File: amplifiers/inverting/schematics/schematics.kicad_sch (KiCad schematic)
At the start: 5 parts, among them J1 15V, U1 LM741

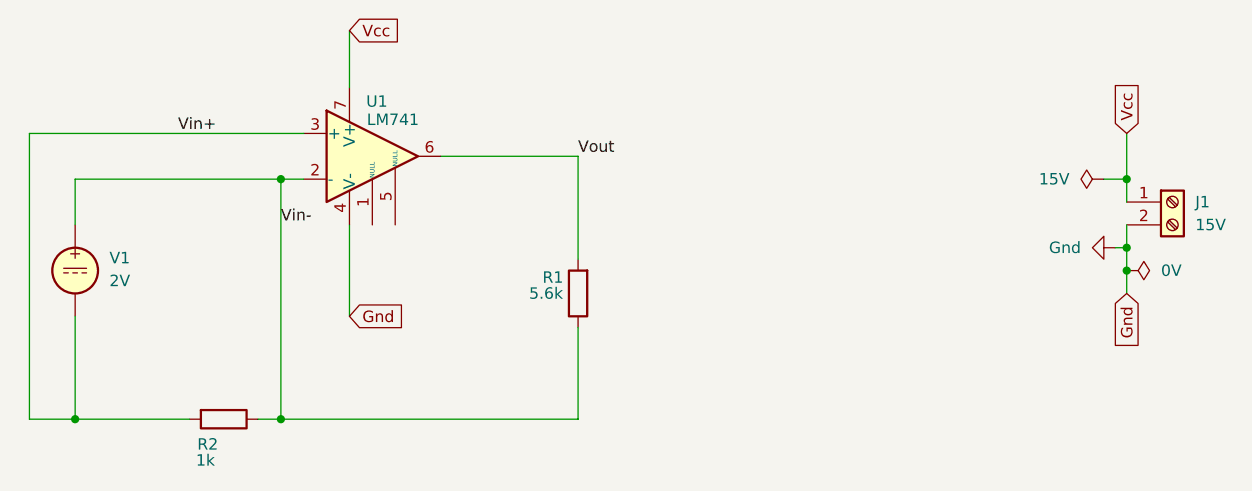
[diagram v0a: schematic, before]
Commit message: docs: add inverting amplifier practical measurements and schematics
Adds practical measurement data and schematics for the inverting
amplifier project. Includes oscilloscope screenshots and measurement
spreadsheet to enhance documentation and provide reference for future
work. Updates GitHub Pages to reflect these additions.

Breaking changes: None

Resolves: None
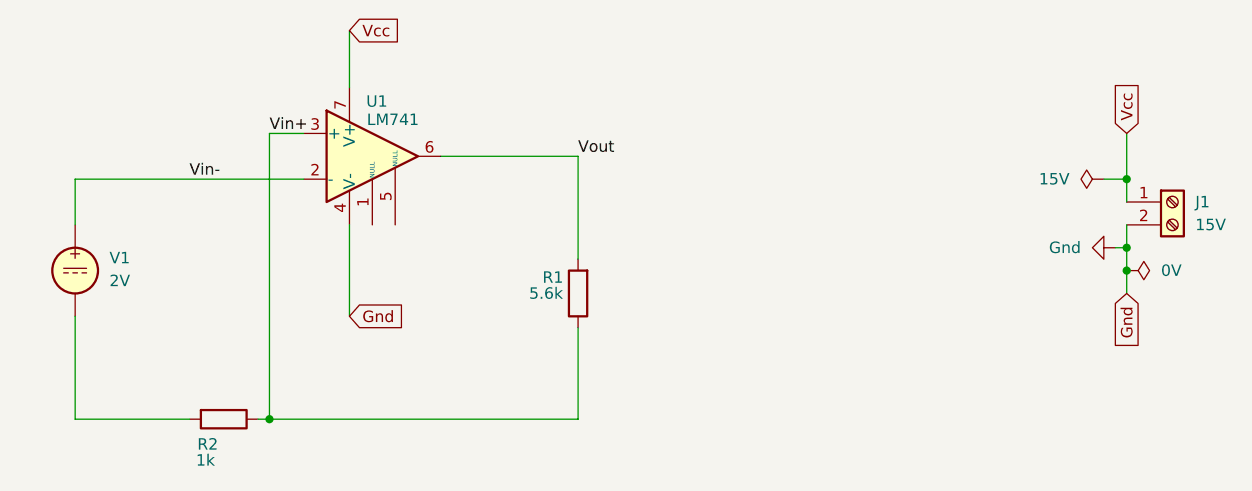
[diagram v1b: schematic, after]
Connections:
- net Vin+: now also R1.1, R2.1; no longer R2.2, V1.2
- net Vin-: no longer R1.1, R2.1
- new net: R2.2, V1.2
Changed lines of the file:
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@@
 	(paper "A5")
 	(junction
-		(at 43.18 33.02)
-		(diameter 0)
-		(color 0 0 0 0)
-	)
-	(junction
-		(at 20.32 59.69)
-		(diameter 0)
-		(color 0 0 0 0)
-	)
-	(junction
-		(at 43.18 59.69)
+		(at 41.91 59.69)
 		(diameter 0)
 		(color 0 0 0 0)
@@
 	(wire
 		(pts
+			(xy 41.91 59.69) (xy 76.2 59.69)
+		)
+		(stroke
+			(width 0)
+			(type default)
+		)
+	)
+	(wire
+		(pts
+			(xy 50.8 48.26) (xy 50.8 38.1)
+		)
+		(stroke
+			(width 0)
+			(type default)
+		)
+	)
+	(wire
+		(pts
 			(xy 20.32 48.26) (xy 20.32 59.69)
 		)
@@
 	(wire
 		(pts
-			(xy 50.8 48.26) (xy 50.8 38.1)
-		)
-		(stroke
-			(width 0)
-			(type default)
-		)
-	)
-	(wire
-		(pts
 			(xy 137.16 27.94) (xy 137.16 33.02)
 		)
@@
 	(wire
 		(pts
-			(xy 15.24 59.69) (xy 20.32 59.69)
-		)
-		(stroke
-			(width 0)
-			(type default)
-		)
-	)
-	(wire
-		(pts
-			(xy 15.24 27.94) (xy 15.24 59.69)
-		)
-		(stroke
-			(width 0)
-			(type default)
-		)
-	)
-	(wire
-		(pts
 			(xy 137.16 43.18) (xy 137.16 45.72)
 		)
@@
 	(wire
 		(pts
-			(xy 43.18 59.69) (xy 76.2 59.69)
+			(xy 40.64 59.69) (xy 41.91 59.69)
+		)
+		(stroke
+			(width 0)
+			(type default)
+		)
+	)
+	(wire
+		(pts
+			(xy 20.32 33.02) (xy 20.32 38.1)
 		)
 		(stroke
@@
 	(wire
 		(pts
-			(xy 43.18 33.02) (xy 45.72 33.02)
-		)
-		(stroke
-			(width 0)
-			(type default)
-		)
-	)
-	(wire
-		(pts
 			(xy 134.62 33.02) (xy 137.16 33.02)
 		)
@@
 	(wire
 		(pts
-			(xy 40.64 59.69) (xy 43.18 59.69)
-		)
-		(stroke
-			(width 0)
-			(type default)
-		)
-	)
-	(wire
-		(pts
-			(xy 20.32 33.02) (xy 43.18 33.02)
+			(xy 41.91 27.94) (xy 41.91 59.69)
 		)
 		(stroke
@@
 	(wire
 		(pts
-			(xy 45.72 27.94) (xy 15.24 27.94)
+			(xy 45.72 27.94) (xy 41.91 27.94)
 		)
 		(stroke
@@
 	(wire
 		(pts
-			(xy 20.32 38.1) (xy 20.32 33.02)
+			(xy 20.32 33.02) (xy 45.72 33.02)
 		)
 		(stroke
@@
 		)
 	)
-	(wire
-		(pts
-			(xy 43.18 59.69) (xy 43.18 33.02)
-		)
-		(stroke
-			(width 0)
-			(type default)
-		)
-	)
 	(label "Vin-"
-		(at 43.18 38.1 0)
+		(at 33.02 33.02 0)
 		(effects
 			(font
@@
 	)
 	(label "Vin+"
-		(at 31.75 27.94 0)
+		(at 41.91 27.94 0)
 		(effects
 			(font

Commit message: docs: update schematics.prl files for inverting and non-inverting amplifiers
Updated the schematics.prl files for both inverting and non-inverting
amplifiers to ensure proper referencing of all components and
connections. This update improves the accuracy of the schematic
representations and enhances the overall documentation quality.

Breaking changes: None

Resolves: None
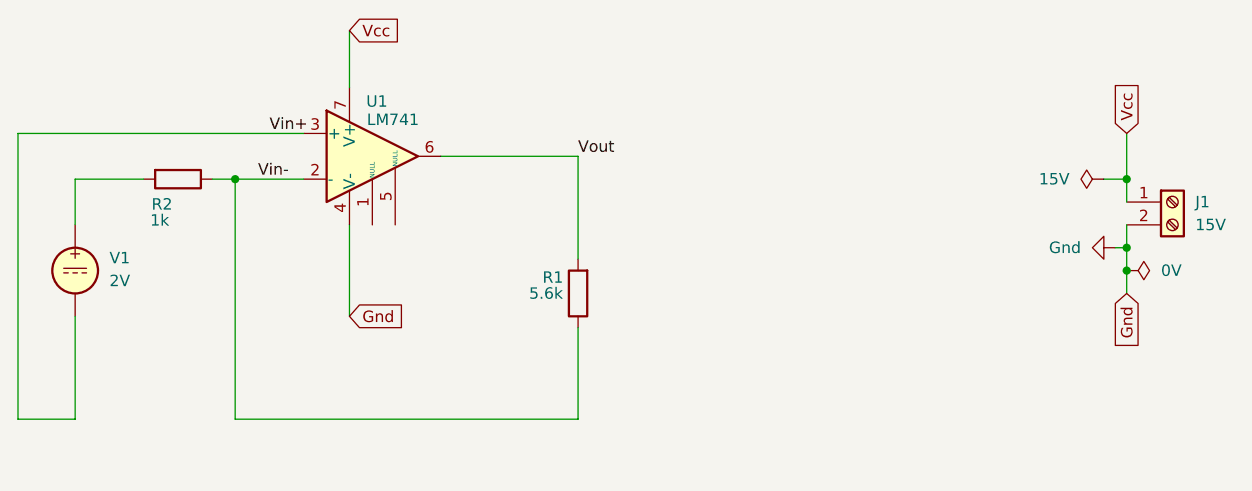
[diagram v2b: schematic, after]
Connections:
- net Vin+: now also V1.2; no longer R1.1, R2.1
- net Vin-: now also R1.1, R2.1; no longer V1.1
- net at R2.2: now also V1.1; no longer V1.2
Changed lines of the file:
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@@
 	(paper "A5")
 	(junction
-		(at 41.91 59.69)
+		(at 38.1 33.02)
 		(diameter 0)
 		(color 0 0 0 0)
@@
 	(wire
 		(pts
-			(xy 41.91 59.69) (xy 76.2 59.69)
+			(xy 35.56 33.02) (xy 38.1 33.02)
+		)
+		(stroke
+			(width 0)
+			(type default)
+		)
+	)
+	(wire
+		(pts
+			(xy 38.1 59.69) (xy 76.2 59.69)
+		)
+		(stroke
+			(width 0)
+			(type default)
+		)
+	)
+	(wire
+		(pts
+			(xy 13.97 59.69) (xy 20.32 59.69)
 		)
 		(stroke
@@
 	(wire
 		(pts
+			(xy 13.97 27.94) (xy 45.72 27.94)
+		)
+		(stroke
+			(width 0)
+			(type default)
+		)
+	)
+	(wire
+		(pts
+			(xy 20.32 33.02) (xy 27.94 33.02)
+		)
+		(stroke
+			(width 0)
+			(type default)
+		)
+	)
+	(wire
+		(pts
 			(xy 137.16 43.18) (xy 137.16 45.72)
 		)
@@
 	(wire
 		(pts
-			(xy 40.64 59.69) (xy 41.91 59.69)
-		)
-		(stroke
-			(width 0)
-			(type default)
-		)
-	)
-	(wire
-		(pts
 			(xy 20.32 33.02) (xy 20.32 38.1)
 		)
@@
 	(wire
 		(pts
-			(xy 20.32 59.69) (xy 33.02 59.69)
-		)
-		(stroke
-			(width 0)
-			(type default)
-		)
-	)
-	(wire
-		(pts
 			(xy 134.62 33.02) (xy 137.16 33.02)
 		)
@@
 	(wire
 		(pts
+			(xy 38.1 59.69) (xy 38.1 33.02)
+		)
+		(stroke
+			(width 0)
+			(type default)
+		)
+	)
+	(wire
+		(pts
 			(xy 50.8 16.51) (xy 50.8 22.86)
 		)
@@
 	(wire
 		(pts
-			(xy 41.91 27.94) (xy 41.91 59.69)
-		)
-		(stroke
-			(width 0)
-			(type default)
-		)
-	)
-	(wire
-		(pts
 			(xy 76.2 30.48) (xy 76.2 41.91)
 		)
@@
 	(wire
 		(pts
-			(xy 45.72 27.94) (xy 41.91 27.94)
+			(xy 38.1 33.02) (xy 45.72 33.02)
 		)
 		(stroke
@@
 	(wire
 		(pts
+			(xy 13.97 27.94) (xy 13.97 59.69)
+		)
+		(stroke
+			(width 0)
+			(type default)
+		)
+	)
+	(wire
+		(pts
 			(xy 60.96 30.48) (xy 76.2 30.48)
 		)
@@
 	(wire
 		(pts
-			(xy 20.32 33.02) (xy 45.72 33.02)
-		)
-		(stroke
-			(width 0)
-			(type default)
-		)
-	)
-	(wire
-		(pts
 			(xy 76.2 49.53) (xy 76.2 59.69)
 		)
@@
 	)
 	(label "Vin-"
-		(at 33.02 33.02 0)
+		(at 40.64 33.02 0)
 		(effects
 			(font
@@
 				(justify right)
 				(hide yes)
-			)
-		)
-	)
-	(symbol
-		(lib_id "Device:R")
-		(at 36.83 59.69 270)
-		(unit 1)
-		(exclude_from_sim no)
-		(in_bom yes)
-		(on_board yes)
-		(dnp no)
-		(property "Reference" "R2"
-			(at 35.052 62.484 90)
-			(effects
-				(font
-					(size 1.27 1.27)
-				)
-			)
-		)
-		(property "Value" "1k"
-			(at 34.798 64.262 90)
-			(effects
-				(font
-					(size 1.27 1.27)
-				)
-			)
-		)
-		(property "Footprint" ""
-			(at 36.83 57.912 90)
-			(effects
-				(font
-					(size 1.27 1.27)
-				)
-				(hide yes)
-			)
-		)
-		(property "Datasheet" "~"
-			(at 36.83 59.69 0)
-			(effects
-				(font
-					(size 1.27 1.27)
-				)
-				(hide yes)
-			)
-		)
-		(property "Description" "Resistor"
-			(at 36.83 59.69 0)
-			(effects
-				(font
-					(size 1.27 1.27)
-				)
-				(hide yes)
-			)
-		)
-		(pin "2"
-		)
-		(pin "1"
-		)
-		(instances
-			(project "differential_amplifier"
-				(path "/872f1d81-1815-459b-9f9e-3f0909be5d1a"
-					(reference "R2")
-					(unit 1)
-				)
 			)
 		)
@@
 					(unit 1)
 				)
+			)
+		)
+	)
+	(symbol
+		(lib_id "Device:R")
+		(at 31.75 33.02 270)
+		(unit 1)
+		(exclude_from_sim no)
+		(in_bom yes)
+		(on_board yes)
+		(dnp no)
+		(property "Reference" "R2"
+			(at 29.972 35.814 90)
+			(effects
+				(font
+					(size 1.27 1.27)
+				)
+			)
+		)
+		(property "Value" "1k"
+			(at 29.718 37.592 90)
+			(effects
+				(font
+					(size 1.27 1.27)
+				)
+			)
+		)
+		(property "Footprint" ""
+			(at 31.75 31.242 90)
+			(effects
+				(font
+					(size 1.27 1.27)
+				)
+				(hide yes)
+			)
+		)
+		(property "Datasheet" "~"
+			(at 31.75 33.02 0)
+			(effects
+				(font
+					(size 1.27 1.27)
+				)
+				(hide yes)
+			)
+		)
+		(property "Description" "Resistor"
+			(at 31.75 33.02 0)
+			(effects
+				(font
+					(size 1.27 1.27)
+				)
+				(hide yes)
+			)
+		)
+		(pin "2"
+		)
+		(pin "1"
+		)
+		(instances
+			(project "schematics"
+				(path "/872f1d81-1815-459b-9f9e-3f0909be5d1a"
+					(reference "R2")
+					(unit 1)
+				)
